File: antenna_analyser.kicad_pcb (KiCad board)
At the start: 2 copper layers, 100 x 50 mm, 32 parts, among them IC1 MCP6002, IC2 ARDUINO_PRO_MINI_3.3V, P1 AD9850_CONN, P2 CONN_LCD, P4 BNC, U1 AMS1117

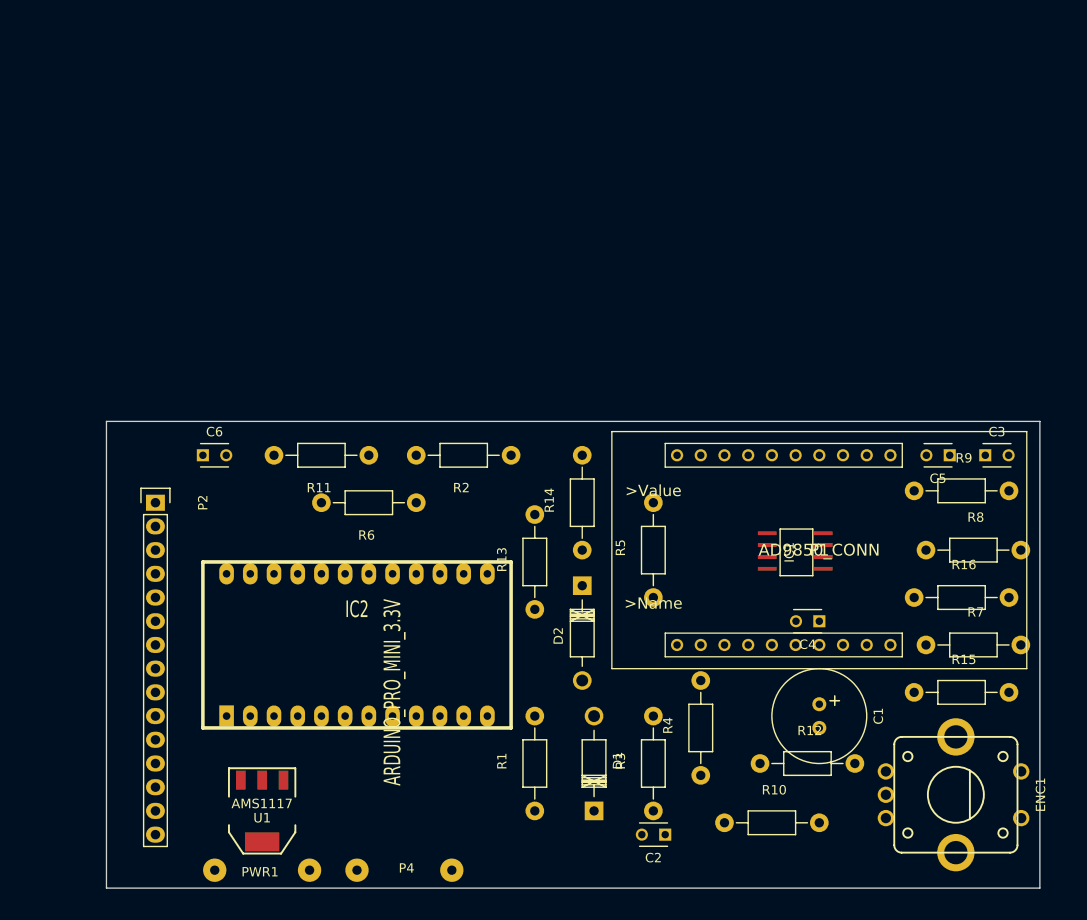
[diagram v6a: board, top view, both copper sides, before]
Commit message: 50/5k ohm resistors
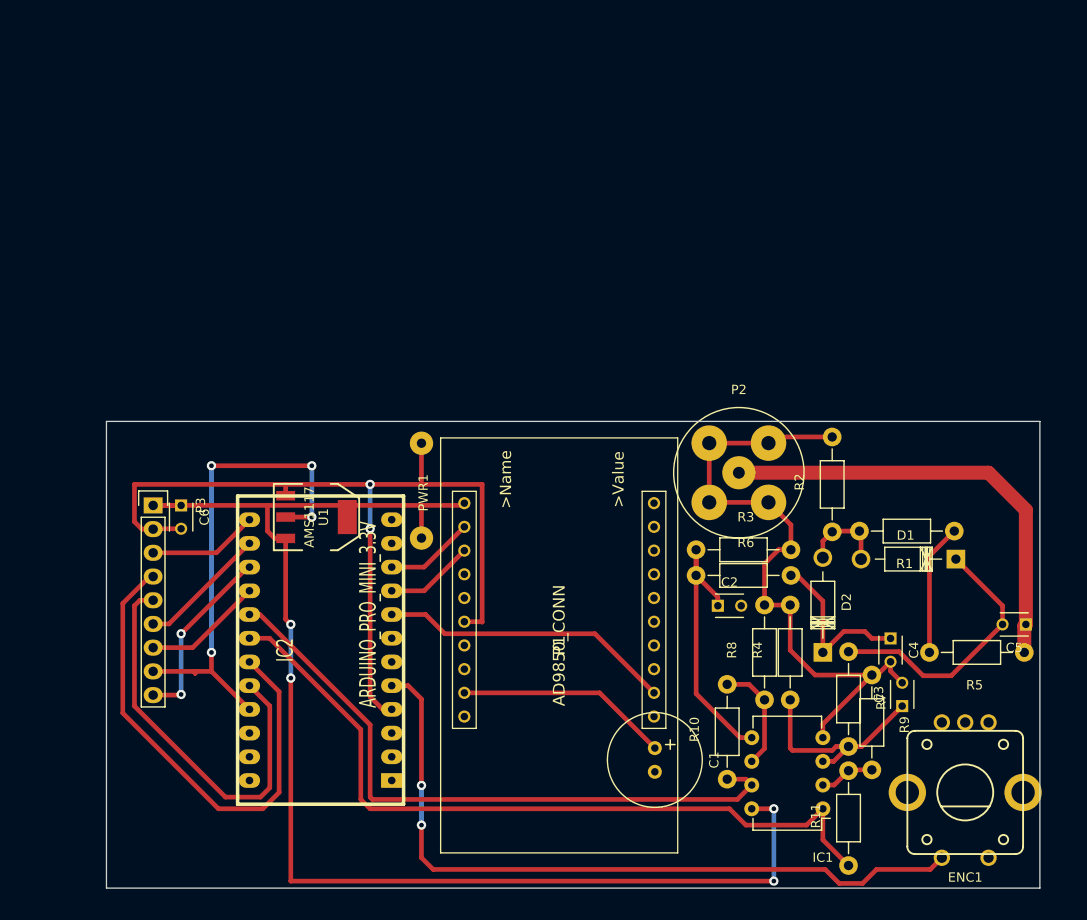
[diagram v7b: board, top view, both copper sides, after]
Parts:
- removed P4: BNC, Wire_Connections_Bridges:WireConnection_1mmDrill
- removed R12: 100, Resistors_ThroughHole:Resistor_Horizontal_RM10mm
- removed R13, R14, R15, R16: 10k, Resistors_ThroughHole:Resistor_Horizontal_RM10mm
- added P3: CONN_LCD, Socket_Strips:Socket_Strip_Straight_1x09, F.Cu at (95.0, 93.0)
- C2: value 100n -> 10n
- C5: value 10n -> 100n
- IC1: footprint sop8:SOP-8 -> Housings_DIP:DIP-8_W7.62mm
- P2: value CONN_LCD -> BNC; footprint Socket_Strips:Socket_Strip_Straight_1x15 -> Connect:bnc-ci
- R1, R2: value 100 -> 50
- R10: value 100 -> 5k
- R11: value 648 -> 5k
- R3: value 100 -> 100k
- R4: value 10k -> 100k
- R5: value 100k -> 50
- R6: value 100 -> 10k
- R7: value 648 -> 10k
- R8: value 10k -> 648
- R9: value 100k -> 648
- moved R11 68.6 mm to (169.5, 126.5), turned to 90 degrees
- moved P2 62.6 mm to (157.8, 89.5), turned to 0 degrees
- moved D1 47.2 mm to (181.0, 98.8), turned to 180 degrees
- moved R1 47.0 mm to (175.8, 95.8), turned to 180 degrees
- moved PWR1 41.9 mm to (123.8, 96.5), turned to 90 degrees
- moved R6 40.9 mm to (158.2, 100.5), turned to 0 degrees
- moved R2 39.6 mm to (167.8, 90.8), turned to 90 degrees
- moved R5 36.4 mm to (183.2, 108.8), turned to 180 degrees
- moved U1 32.0 mm to (112.5, 94.2), turned to 270 degrees
- moved P1 29.7 mm to (138.5, 108.0), turned to 270 degrees
- moved C3 28.3 mm to (175.2, 114.5), turned to 90 degrees
- moved D2 26.8 mm to (166.8, 108.8), turned to 90 degrees
- moved R9 26.6 mm to (172.0, 116.2), turned to 270 degrees
- moved IC1 25.8 mm to (166.8, 125.5), turned to 180 degrees
- moved C2 25.2 mm to (155.5, 103.8), turned to 0 degrees
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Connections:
- C2 pad 2: Net-(C2-Pad2) -> GND
- C5 pad 2: GND -> Net-(C5-Pad2)
- D1 pad 1: Net-(C2-Pad2) -> Net-(C5-Pad2)
- IC1 pad 5: Net-(C5-Pad1) -> Net-(C2-Pad1)
- P1 pad 11: GND -> Net-(P1-Pad11)
- P1 pad 13: GND -> Net-(P1-Pad13)
- P1 pad 14: GND -> Net-(P1-Pad14)
- P1 pad 15: GND -> Net-(P1-Pad15)
- P1 pad 16: GND -> Net-(P1-Pad16)
- P1 pad 17: GND -> Net-(P1-Pad17)
- P1 pad 18: GND -> Net-(P1-Pad18)
- P1 pad 19: GND -> Net-(P1-Pad19)
- P1 pad 20: +5V -> Net-(P1-Pad20)
- P2 pad 1: +5V -> Net-(C5-Pad1)
- R10 pad 1: Net-(C2-Pad1) -> Net-(IC1-Pad7)
- R10 pad 2: Net-(C1-Pad2) -> Net-(IC1-Pad6)
- R11 pad 1: Net-(IC1-Pad6) -> Net-(IC1-Pad1)
- R11 pad 2: GND -> Net-(IC1-Pad2)
- R3 pad 1: Net-(C1-Pad2) -> Net-(C2-Pad1)
- R3 pad 2: Net-(D1-Pad2) -> GND
- R4 pad 1: Net-(C2-Pad2) -> Net-(C3-Pad1)
- R4 pad 2: Net-(C3-Pad1) -> GND
- R5 pad 1: Net-(C3-Pad1) -> Net-(C5-Pad1)
- R5 pad 2: GND -> Net-(C1-Pad2)
- R6 pad 1: Net-(D1-Pad2) -> Net-(C2-Pad1)
- R6 pad 2: GND -> Net-(C4-Pad1)
- R7 pad 1: GND -> Net-(C5-Pad2)
- R7 pad 2: Net-(IC1-Pad2) -> Net-(C3-Pad1)
- R8 pad 1: Net-(C5-Pad1) -> Net-(IC1-Pad6)
- R8 pad 2: Net-(C4-Pad1) -> GND
- R9 pad 1: Net-(C5-Pad1) -> GND
- R9 pad 2: GND -> Net-(IC1-Pad2)
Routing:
- net GND: track 0.00 -> 166.3 mm, vias 0 -> 2
- net +5V: track 0.00 -> 143.8 mm, vias 0 -> 4
- net Net-(IC1-Pad1): track 0.00 -> 82.1 mm
- net Net-(ENC1-PadSW2): track 0.00 -> 78.8 mm, vias 0 -> 2
- net Net-(IC1-Pad7): track 0.00 -> 70.1 mm
- net Net-(IC2-Pad21): track 0.00 -> 54.3 mm, vias 0 -> 4
- net Net-(IC2-Pad19): track 0.00 -> 53.8 mm
- net Net-(C5-Pad1): track 0.00 -> 47.7 mm
- net Net-(IC2-Pad20): track 0.00 -> 43.8 mm
- net Net-(IC2-Pad8): track 0.00 -> 31.6 mm
- net Net-(C2-Pad1): track 0.00 -> 30.3 mm
- net Net-(C5-Pad2): track 0.00 -> 28.9 mm
- net Net-(C1-Pad1): track 0.00 -> 22.9 mm
- net Net-(C3-Pad1): track 0.00 -> 22.6 mm
- net Net-(IC2-Pad15): track 0.00 -> 19.8 mm, vias 0 -> 2
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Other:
- net class ANT added: clearance 0.25, trace_width 1.5, via_dia 1, via_drill 0.5
- net class Default: clearance 0.3 -> 0.25; trace_width 0.3 -> 0.5; via_dia 0.6 -> 1; via_drill 0.4 -> 0.5
- rule trace_clearance: 0.3 -> 0.25

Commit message: Track laying, cont'd.
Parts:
- moved C6 82.8 mm to (177.5, 116.0), turned to 0 degrees
- moved R6 35.9 mm to (184.5, 125.0), turned to 90 degrees
- moved R3 34.3 mm to (179.0, 125.0), turned to 90 degrees
- moved C5 31.5 mm to (157.0, 107.5), turned to 0 degrees
- moved ENC1 30.3 mm to (181.5, 93.5)
- moved C1 29.0 mm to (149.5, 90.0), turned to 0 degrees
- moved R5 28.2 mm to (162.0, 90.2), turned to 0 degrees
- moved C2 26.0 mm to (165.0, 128.0), turned to 180 degrees
- moved C3 22.2 mm to (156.0, 125.5), turned to 270 degrees
- moved R9 22.0 mm to (152.5, 126.5), turned to 90 degrees
- moved D2 21.5 mm to (188.0, 112.0), turned to 180 degrees
- moved R10 17.7 mm to (173.5, 122.0), turned to 270 degrees
- moved PWR1 17.1 mm to (109.5, 87.0), turned to 0 degrees
- moved R11 17.1 mm to (156.0, 116.0), turned to 270 degrees
- moved R7 14.7 mm to (180.5, 104.0), turned to 180 degrees
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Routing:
- net +5V: track 143.8 -> 34.9 mm, vias 4 -> 0
- net GND: track 166.3 -> 249.0 mm, vias 2 -> 0
- net Net-(IC1-Pad1): track 82.1 -> 11.7 mm
- net Net-(IC1-Pad7): track 70.1 -> 12.5 mm
- net Net-(IC2-Pad19): track 53.8 -> 18.3 mm, vias 0 -> 2
- net Net-(IC2-Pad15): track 19.8 -> 51.1 mm, vias 2 -> 0
- net Net-(C5-Pad1): track 47.7 -> 17.3 mm
- net Net-(C3-Pad1): track 22.6 -> 53.0 mm
- net Net-(IC2-Pad20): track 43.8 -> 17.8 mm, vias 0 -> 2
- net Net-(C5-Pad2): track 28.9 -> 5.00 mm
- net Net-(C1-Pad1): track 22.9 -> 39.2 mm, vias 0 -> 2
- net Net-(ENC1-PadSW2): track 78.8 -> 92.4 mm, vias 2 -> 0
- net Net-(IC1-Pad6): track 11.8 -> 21.8 mm
- net Net-(C4-Pad1): track 18.6 -> 9.37 mm
- net Net-(C1-Pad2): track 14.1 -> 22.1 mm
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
